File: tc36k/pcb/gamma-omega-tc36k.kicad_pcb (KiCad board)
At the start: 2 copper layers, 232.8 x 111.4 mm, 45 parts

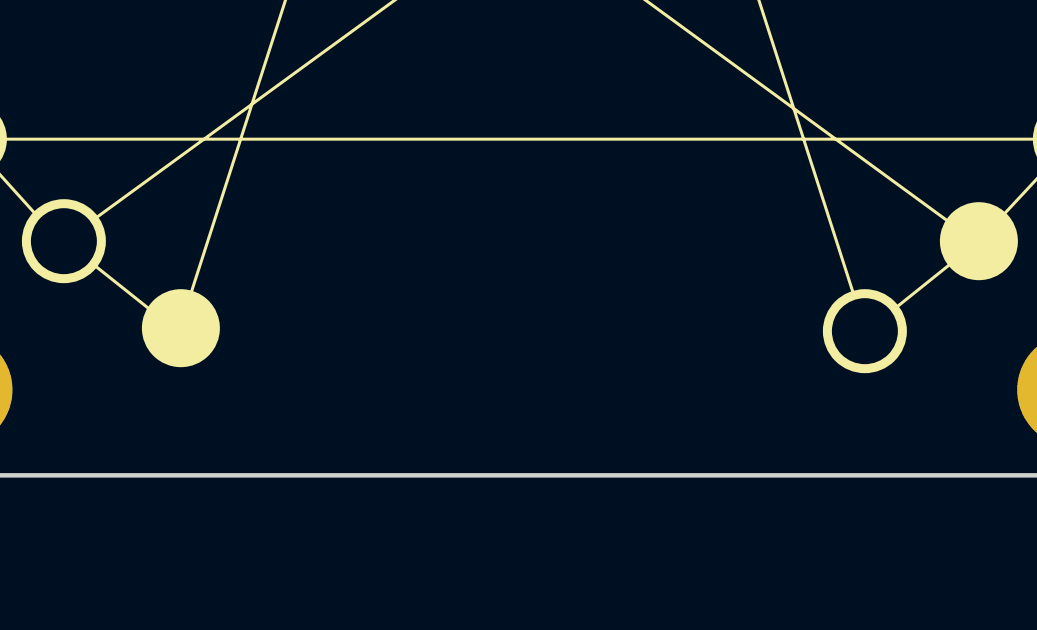
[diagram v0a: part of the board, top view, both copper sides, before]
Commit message: Add label to PCB silkscreen
TC36K: Partial
Tutte-Coxeter
Graph Layout

Centered in bold, 1.6mm default KiCad font.
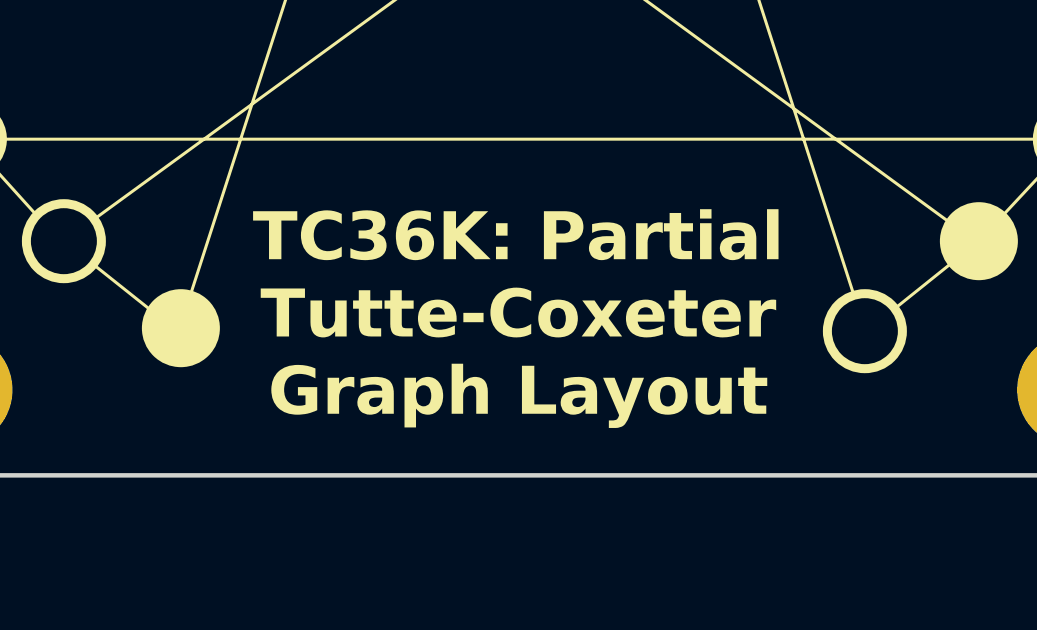
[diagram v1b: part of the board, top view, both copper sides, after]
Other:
- board text added: "TC36K: Partial Tutte-Coxeter Graph Layout"
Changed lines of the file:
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@@
+		)
+	)
+	(gr_text "TC36K: Partial\nTutte-Coxeter\nGraph Layout"
+		(at 158.075 146.975 0)
+		(layer "F.SilkS")
+		(effects
+			(font
+				(size 1.6 1.6)
+				(thickness 0.32)
+				(bold yes)
+			)
+			(justify top)
+		)
+	)
+	(gr_text "TC36K: Partial\nTutte-Coxeter\nGraph Layout"
+		(at 158.075 147 -0)
+		(layer "B.SilkS")
+		(effects
+			(font
+				(size 1.6 1.6)
+				(thickness 0.32)
+				(bold yes)
+			)
+			(justify top mirror)
 		)
 	)
